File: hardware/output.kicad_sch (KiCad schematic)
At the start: 12 parts

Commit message: Fixed Logic
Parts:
- added K?: DIPxx-2Axx-21x, Relay_THT:Relay_StandexMeder_DIP_LowProfile, symbol Relay:DIPxx-2Axx-21x
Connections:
- net VALVE_1_OUT renamed VALVE_1-
- net VALVE_2_OUT renamed VALVE_2-
- new net AIR+: K?.6
- new net AIR-: K?.2
- new net VALVE_1+: K?.1
- new net VALVE_2+: K?.14
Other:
- note added: "Solenoid (Normally opened valve)"
- note added: "Solenoid low side switches"
- note removed: "Valve coils ground low side switches, other side of valve coils tied to supply Voltage"
- moved on the sheet: C?, D?, Q?, R?

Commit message: Alpha 1.0.0 Schematic
First Schematic Version for initial checkup
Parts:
- removed C? (x2): C, symbol Device:C
- removed D? (x2): D_Schottky, symbol Device:D_Schottky
- removed D? (x2): D_Zener, symbol Device:D_Zener
- added D?: D_Schottky, symbol Device:D_Schottky
- R? (x2): value R -> 10k
- R? (x2): value R -> 1k
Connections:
- net AIR+: now also D?.1 (K)
- net AIR-: now also D?.2 (A)
- net at Q?.1 (G), R?.1: now also R?.1 (x2)
- net LINE: now reaches K?.7
- net LINE: now also K?.8
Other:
- note added: "LINE means supply connected After LVMS-> ASMS-> RES-> 2 Required by T15 2.2"
- moved on the sheet: R?

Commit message: Minor changes on v1 schematic
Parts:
- D?: value D_Schottky -> SK54BL
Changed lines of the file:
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@@
       (effects (font (size 1.27 1.27)) (justify left))
     )
-    (property "Value" "D_Schottky" (id 1) (at 148.59 61.9124 90)
+    (property "Value" "SK54BL" (id 1) (at 148.59 61.9124 90)
       (effects (font (size 1.27 1.27)) (justify left))
     )

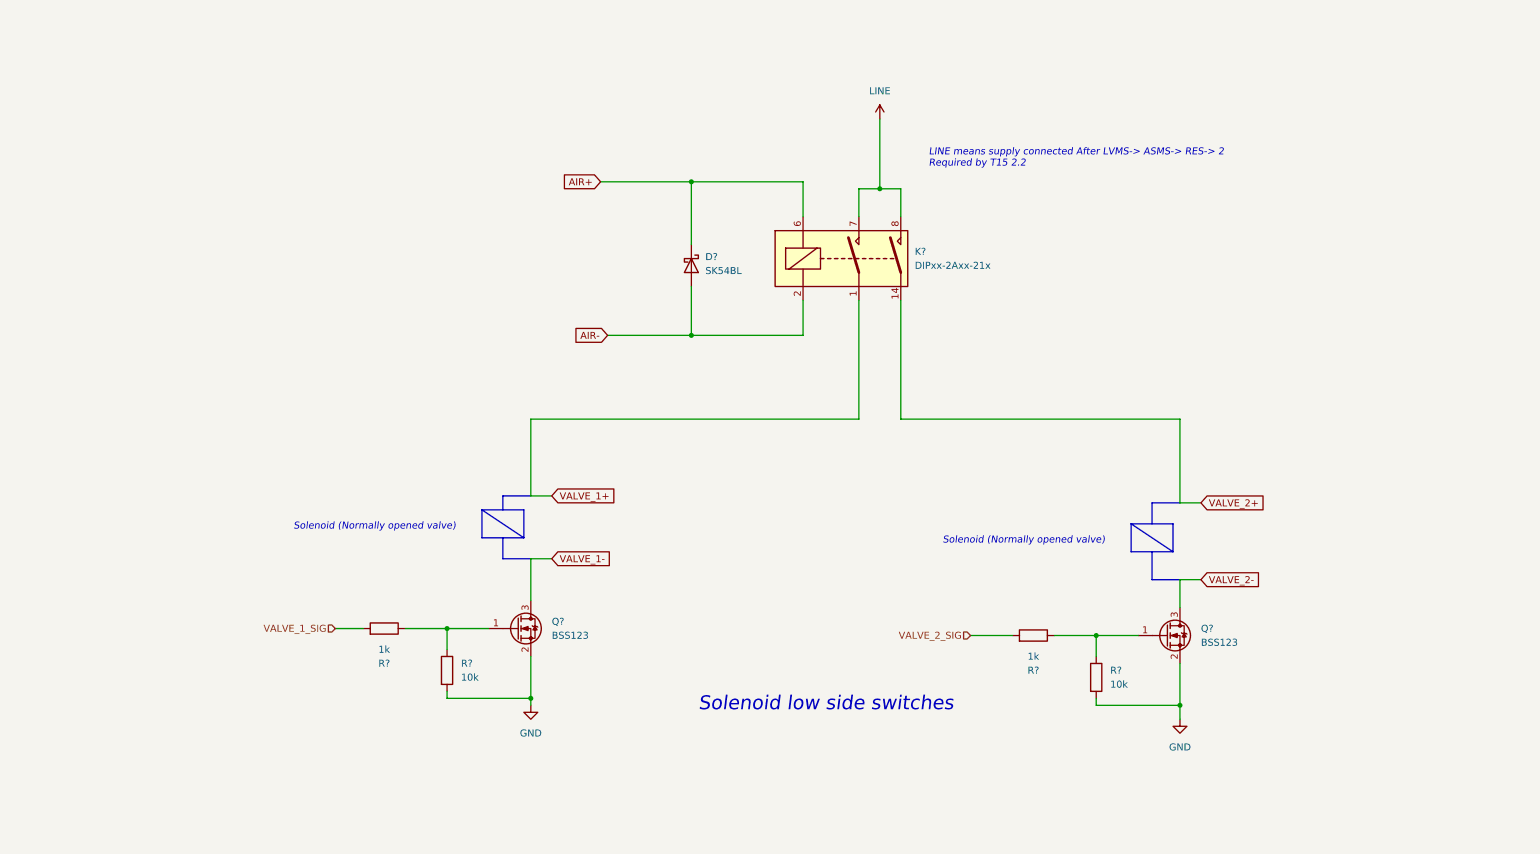
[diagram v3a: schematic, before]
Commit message: minor schematic cleanup
Fixes before second review
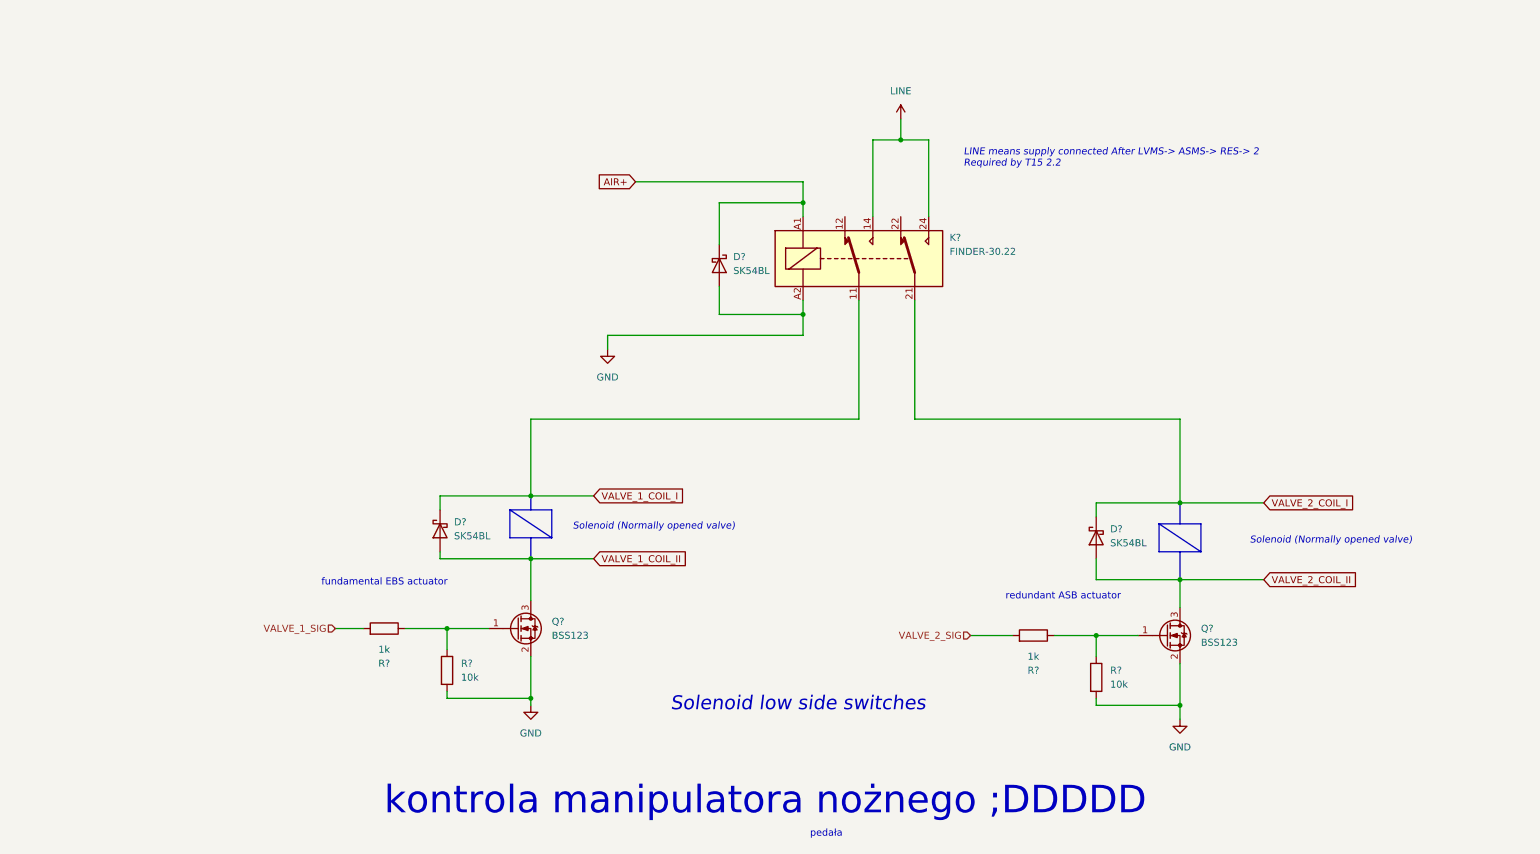
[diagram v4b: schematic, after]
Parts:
- added D? (x2): SK54BL, Diode_SMD:D_SMB, symbol Device:D_Schottky
- K?: value DIPxx-2Axx-21x -> FINDER-30.22; footprint Relay_THT:Relay_StandexMeder_DIP_LowProfile -> Relay_THT:Relay_DPDT_Finder_30.22; symbol Relay:DIPxx-2Axx-21x -> Relay:FINDER-30.22
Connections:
- net VALVE_2+ is gone; now on net LINE: K?.14
- net AIR+: now also K?.A1; no longer K?.6
- net GND: now also D?.2 (A), K?.A2
- net LINE: now also K?.24; no longer K?.7, K?.8
- removed net AIR-: D?.2 (A), K?.2
- removed net VALVE_1+: K?.1
- net VALVE_1- renamed VALVE_1_COIL_II
- net VALVE_1_COIL_II: now also D?.2 (A)
- net VALVE_2- renamed VALVE_2_COIL_II
- net VALVE_2_COIL_II: now also D?.2 (A)
- new net VALVE_1_COIL_I: D?.1 (K), K?.11
- new net VALVE_2_COIL_I: D?.1 (K), K?.21
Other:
- note added: "fundamental EBS actuator"
- note added: "kontrola manipulatora nożnego ;DDDDD"
- note added: "pedała"
- note added: "redundant ASB actuator"
- company: (none) -> PUT Motorsport
- title: (none) -> EBS, and ASB redunant actuators Supply and Control
- moved on the sheet: D?

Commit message: Schematic ready for second review
Cleaned up, numerated, added footprints, JW notes considered
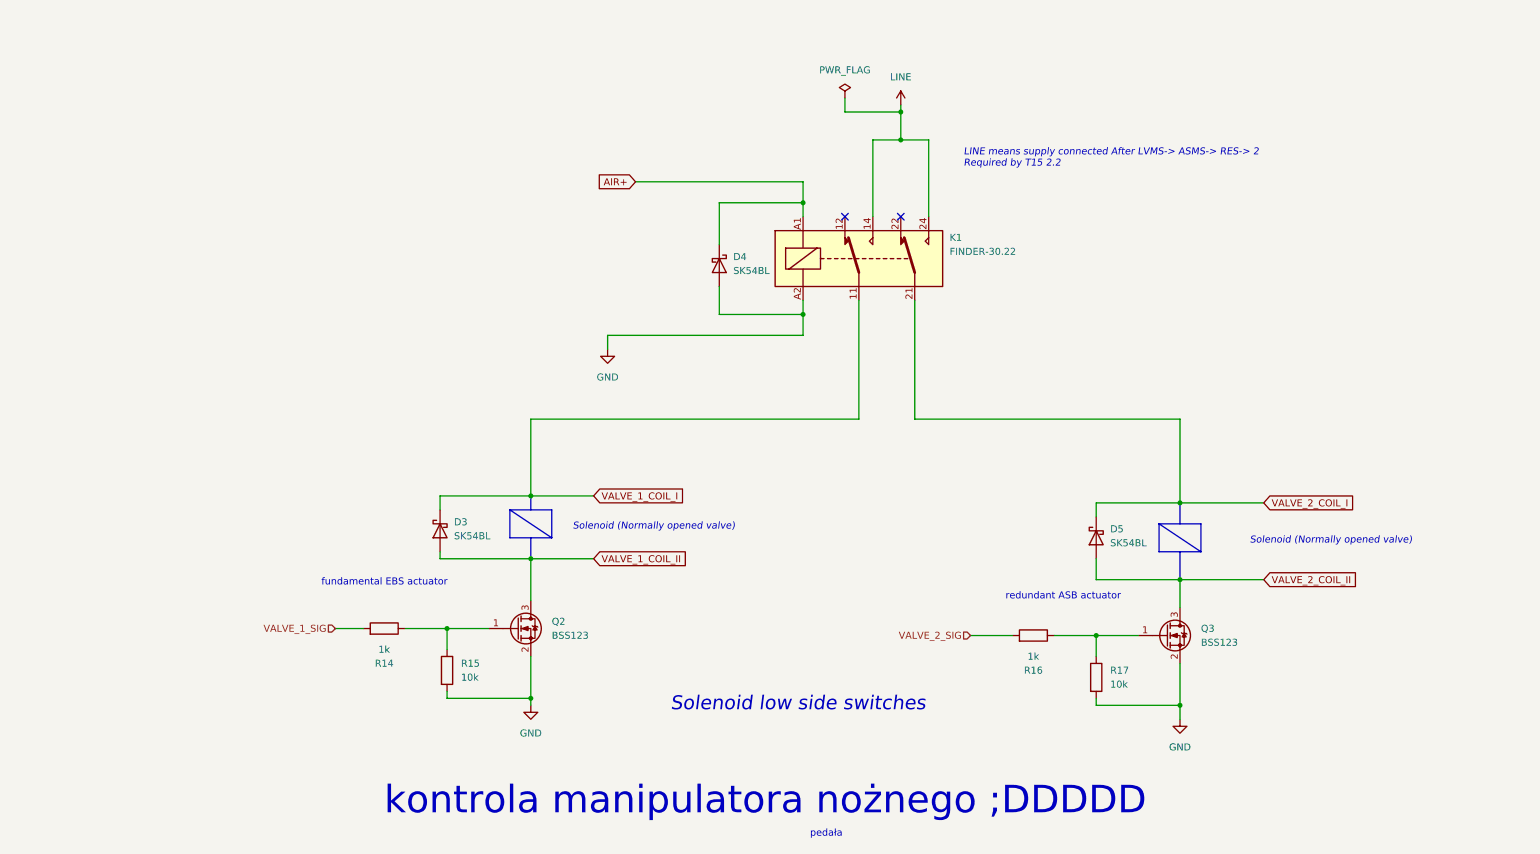
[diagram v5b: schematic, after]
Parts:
- D4: renamed from D?; footprint (none) -> Diode_SMD:D_SMB
- R14, R15, R16, R17: renamed from R?; footprint (none) -> Resistor_SMD:R_0603_1608Metric
- gave numbers to parts that had none: 5
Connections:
- no-connect marks 0 -> 2
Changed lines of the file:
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@@
   (junction (at 101.6 127) (diameter 0) (color 0 0 0 0)
   )
+  (junction (at 184.15 33.02) (diameter 0) (color 0 0 0 0)
+  )
   (junction (at 184.15 38.1) (diameter 0) (color 0 0 0 0)
   )
@@
   (junction (at 166.37 49.53) (diameter 0) (color 0 0 0 0)
   )
+  (no_connect (at 184.15 52.07))
+  (no_connect (at 173.99 52.07))
   (wire (pts (xy 219.71 118.11) (xy 234.95 118.11))
     (stroke (width 0) (type default) (color 0 0 0 0))
@@
     (stroke (width 0) (type default) (color 0 0 0 0))
   )
+  (wire (pts (xy 184.15 33.02) (xy 184.15 38.1))
+    (stroke (width 0) (type default) (color 0 0 0 0))
+  )
   (wire (pts (xy 212.09 128.27) (xy 219.71 128.27))
     (stroke (width 0) (type default) (color 0 0 0 0))
   )
-  (wire (pts (xy 184.15 34.29) (xy 184.15 38.1))
+  (wire (pts (xy 184.15 31.75) (xy 184.15 33.02))
     (stroke (width 0) (type default) (color 0 0 0 0))
   )
@@
     (stroke (width 0) (type default) (color 0 0 0 0))
   )
+  (wire (pts (xy 173.99 33.02) (xy 173.99 30.48))
+    (stroke (width 0) (type default) (color 0 0 0 0))
+  )
   (polyline (pts (xy 116.84 114.3) (xy 116.84 114.3))
     (stroke (width 0) (type default) (color 0 0 0 0))
@@
   )
   (polyline (pts (xy 113.03 105.41) (xy 113.03 110.49))
+    (stroke (width 0) (type default) (color 0 0 0 0))
+  )
+  (wire (pts (xy 184.15 33.02) (xy 173.99 33.02))
     (stroke (width 0) (type default) (color 0 0 0 0))
   )
@@
     (effects (font (size 1.27 1.27)) (justify right))
   )
+  (symbol (lib_id "power:PWR_FLAG") (at 173.99 30.48 0) (unit 1)
+    (in_bom yes) (on_board yes) (fields_autoplaced)
+    (property "Reference" "#FLG0103" (id 0) (at 173.99 28.575 0)
+      (effects (font (size 1.27 1.27)) hide)
+    )
+    (property "Value" "PWR_FLAG" (id 1) (at 173.99 25.4 0))
+    (property "Footprint" "" (id 2) (at 173.99 30.48 0)
+      (effects (font (size 1.27 1.27)) hide)
+    )
+    (property "Datasheet" "~" (id 3) (at 173.99 30.48 0)
+      (effects (font (size 1.27 1.27)) hide)
+    )
+    (pin "1")
+  )
   (symbol (lib_id "Device:R") (at 219.71 135.89 0) (unit 1)
     (in_bom yes) (on_board yes) (fields_autoplaced)
-    (property "Reference" "R?" (id 0) (at 222.25 134.6199 0)
+    (property "Reference" "R17" (id 0) (at 222.25 134.6199 0)
       (effects (font (size 1.27 1.27)) (justify left))
     )
@@
       (effects (font (size 1.27 1.27)) (justify left))
     )
-    (property "Footprint" "" (id 2) (at 217.932 135.89 90)
+    (property "Footprint" "Resistor_SMD:R_0603_1608Metric" (id 2) (at 217.932 135.89 90)
       (effects (font (size 1.27 1.27)) hide)
     )
@@
   (symbol (lib_id "Device:D_Schottky") (at 151.13 60.96 270) (unit 1)
     (in_bom yes) (on_board yes) (fields_autoplaced)
-    (property "Reference" "D?" (id 0) (at 153.67 59.3724 90)
+    (property "Reference" "D4" (id 0) (at 153.67 59.3724 90)
       (effects (font (size 1.27 1.27)) (justify left))
     )
@@
       (effects (font (size 1.27 1.27)) (justify left))
     )
-    (property "Footprint" "" (id 2) (at 151.13 60.96 0)
+    (property "Footprint" "Diode_SMD:D_SMB" (id 2) (at 151.13 60.96 0)
       (effects (font (size 1.27 1.27)) hide)
     )
@@
   (symbol (lib_id "power:GND") (at 116.84 140.97 0) (unit 1)
     (in_bom yes) (on_board yes) (fields_autoplaced)
-    (property "Reference" "#PWR?" (id 0) (at 116.84 147.32 0)
+    (property "Reference" "#PWR030" (id 0) (at 116.84 147.32 0)
       (effects (font (size 1.27 1.27)) hide)
     )
@@
     (pin "1")
   )
-  (symbol (lib_id "power:LINE") (at 184.15 34.29 0) (unit 1)
-    (in_bom yes) (on_board yes) (fields_autoplaced)
-    (property "Reference" "#PWR?" (id 0) (at 184.15 38.1 0)
-      (effects (font (size 1.27 1.27)) hide)
-    )
-    (property "Value" "LINE" (id 1) (at 184.15 29.21 0))
-    (property "Footprint" "" (id 2) (at 184.15 34.29 0)
-      (effects (font (size 1.27 1.27)) hide)
-    )
-    (property "Datasheet" "" (id 3) (at 184.15 34.29 0)
+  (symbol (lib_id "power:LINE") (at 184.15 31.75 0) (unit 1)
+    (in_bom yes) (on_board yes) (fields_autoplaced)
+    (property "Reference" "#PWR032" (id 0) (at 184.15 35.56 0)
+      (effects (font (size 1.27 1.27)) hide)
+    )
+    (property "Value" "LINE" (id 1) (at 184.15 26.67 0))
+    (property "Footprint" "" (id 2) (at 184.15 31.75 0)
+      (effects (font (size 1.27 1.27)) hide)
+    )
+    (property "Datasheet" "" (id 3) (at 184.15 31.75 0)
       (effects (font (size 1.27 1.27)) hide)
     )
@@
   (symbol (lib_id "Device:D_Schottky") (at 219.71 110.49 90) (mirror x) (unit 1)
     (in_bom yes) (on_board yes) (fields_autoplaced)
-    (property "Reference" "D?" (id 0) (at 222.25 108.9024 90)
+    (property "Reference" "D5" (id 0) (at 222.25 108.9024 90)
       (effects (font (size 1.27 1.27)) (justify right))
     )
@@
   (symbol (lib_id "power:GND") (at 234.95 143.51 0) (unit 1)
     (in_bom yes) (on_board yes) (fields_autoplaced)
-    (property "Reference" "#PWR?" (id 0) (at 234.95 149.86 0)
+    (property "Reference" "#PWR033" (id 0) (at 234.95 149.86 0)
       (effects (font (size 1.27 1.27)) hide)
     )
@@
   (symbol (lib_id "Device:D_Schottky") (at 100.33 109.22 90) (mirror x) (unit 1)
     (in_bom yes) (on_board yes) (fields_autoplaced)
-    (property "Reference" "D?" (id 0) (at 102.87 107.6324 90)
+    (property "Reference" "D3" (id 0) (at 102.87 107.6324 90)
       (effects (font (size 1.27 1.27)) (justify right))
     )
@@
   (symbol (lib_id "Transistor_FET:BSS123") (at 232.41 128.27 0) (unit 1)
     (in_bom yes) (on_board yes) (fields_autoplaced)
-    (property "Reference" "Q?" (id 0) (at 238.76 126.9999 0)
+    (property "Reference" "Q3" (id 0) (at 238.76 126.9999 0)
       (effects (font (size 1.27 1.27)) (justify left))
     )
@@
   (symbol (lib_id "Device:R") (at 208.28 128.27 270) (mirror x) (unit 1)
     (in_bom yes) (on_board yes)
-    (property "Reference" "R?" (id 0) (at 208.28 134.62 90))
+    (property "Reference" "R16" (id 0) (at 208.28 134.62 90))
     (property "Value" "1k" (id 1) (at 208.28 132.08 90))
-    (property "Footprint" "" (id 2) (at 208.28 130.048 90)
+    (property "Footprint" "Resistor_SMD:R_0603_1608Metric" (id 2) (at 208.28 130.048 90)
       (effects (font (size 1.27 1.27)) hide)
     )
@@
   (symbol (lib_id "Relay:FINDER-30.22") (at 176.53 59.69 0) (unit 1)
     (in_bom yes) (on_board yes) (fields_autoplaced)
-    (property "Reference" "K?" (id 0) (at 193.04 55.88 0)
+    (property "Reference" "K1" (id 0) (at 193.04 55.88 0)
       (effects (font (size 1.27 1.27)) (justify left))
     )
@@
   (symbol (lib_id "Device:R") (at 90.17 127 270) (mirror x) (unit 1)
     (in_bom yes) (on_board yes)
-    (property "Reference" "R?" (id 0) (at 90.17 133.35 90))
+    (property "Reference" "R14" (id 0) (at 90.17 133.35 90))
     (property "Value" "1k" (id 1) (at 90.17 130.81 90))
-    (property "Footprint" "" (id 2) (at 90.17 128.778 90)
+    (property "Footprint" "Resistor_SMD:R_0603_1608Metric" (id 2) (at 90.17 128.778 90)
       (effects (font (size 1.27 1.27)) hide)
     )
@@
   (symbol (lib_id "Device:R") (at 101.6 134.62 0) (unit 1)
     (in_bom yes) (on_board yes) (fields_autoplaced)
-    (property "Reference" "R?" (id 0) (at 104.14 133.3499 0)
+    (property "Reference" "R15" (id 0) (at 104.14 133.3499 0)
       (effects (font (size 1.27 1.27)) (justify left))
     )
@@
       (effects (font (size 1.27 1.27)) (justify left))
     )
-    (property "Footprint" "" (id 2) (at 99.822 134.62 90)
+    (property "Footprint" "Resistor_SMD:R_0603_1608Metric" (id 2) (at 99.822 134.62 90)
       (effects (font (size 1.27 1.27)) hide)
     )
@@
   (symbol (lib_id "power:GND") (at 130.81 76.2 0) (unit 1)
     (in_bom yes) (on_board yes) (fields_autoplaced)
-    (property "Reference" "#PWR?" (id 0) (at 130.81 82.55 0)
+    (property "Reference" "#PWR031" (id 0) (at 130.81 82.55 0)
       (effects (font (size 1.27 1.27)) hide)
     )
@@
   (symbol (lib_id "Transistor_FET:BSS123") (at 114.3 127 0) (unit 1)
     (in_bom yes) (on_board yes) (fields_autoplaced)
-    (property "Reference" "Q?" (id 0) (at 120.65 125.7299 0)
-      (effects (font (size 1.27 1.27)) (justify left))
-    )
+    (property "Reference" "Q2" (id 0) (at 120.65 125.7299 0)
+      (effects (font (size 1.27 1.27)) (justify left))
+    )

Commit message: 0xERC State
Schematic needs only simulation and veryfying component choice for now
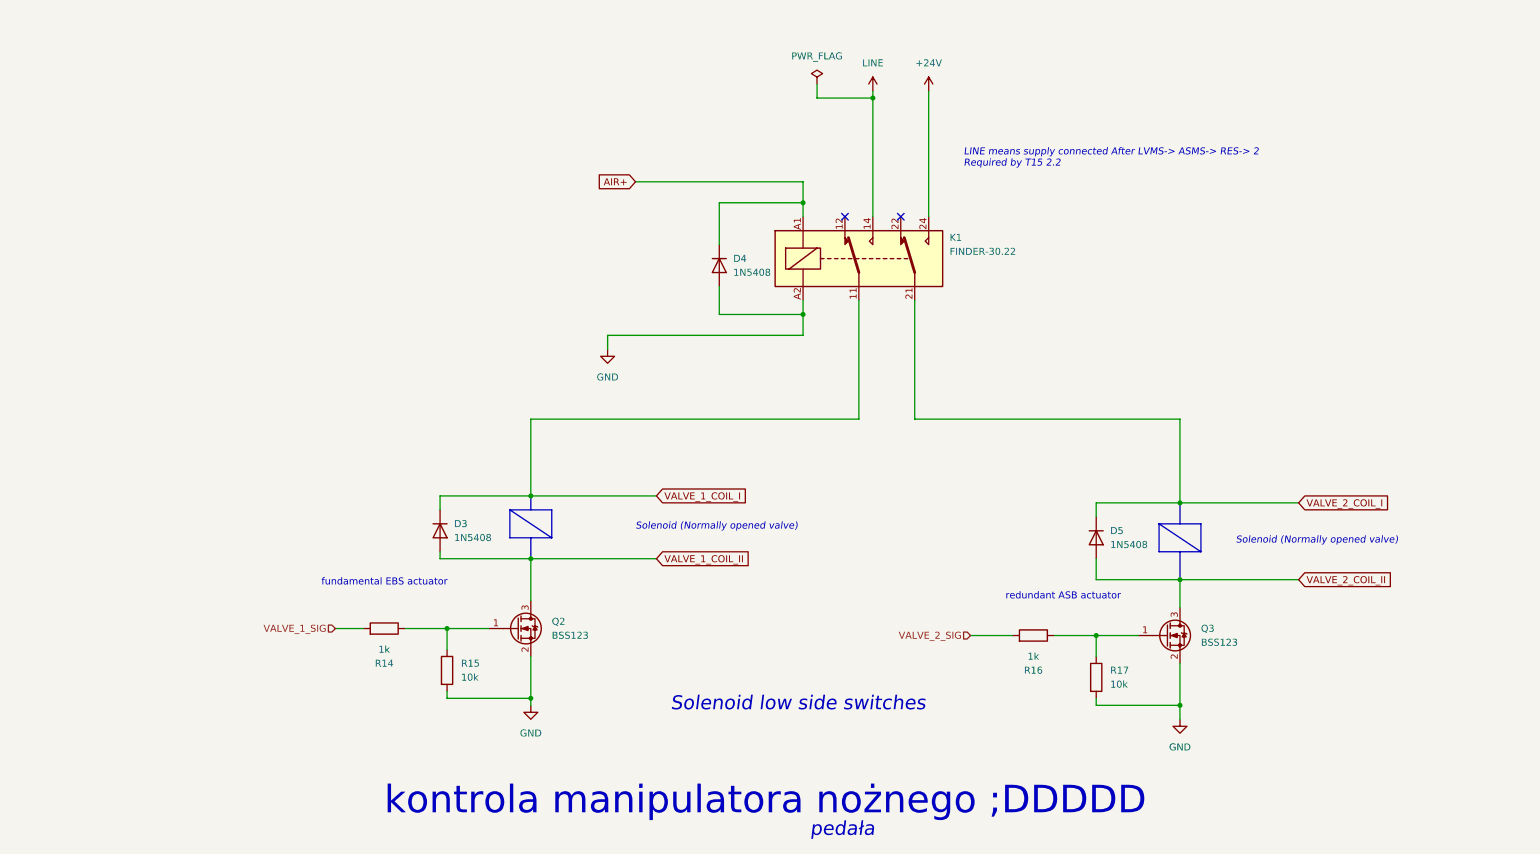
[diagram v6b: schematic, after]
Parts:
- removed D3, D4, D5: SK54BL, Diode_SMD:D_SMB, symbol Device:D_Schottky
- added D3, D4, D5: 1N5408, Diode_THT:D_DO-201AD_P15.24mm_Horizontal, symbol Diode:1N5408
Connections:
- net AIR+: now also D4.1 (K)
- net GND: now also D4.2 (A)
- net LINE: no longer K1.24
- net VALVE_1_COIL_I: now also D3.1 (K)
- net VALVE_1_COIL_II: now also D3.2 (A)
- net VALVE_2_COIL_I: now also D5.1 (K)
- net VALVE_2_COIL_II: now also D5.2 (A)
- new net +24V: K1.24
